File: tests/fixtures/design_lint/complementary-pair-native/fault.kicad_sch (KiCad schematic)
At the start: 1 part, among them J1 Synthetic USB SuperSpeed conn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

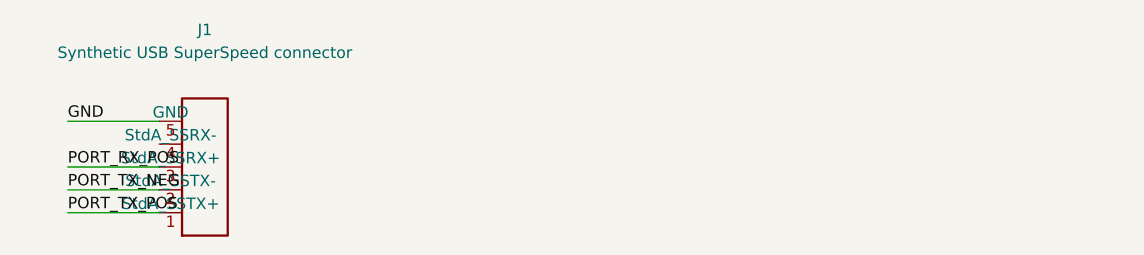
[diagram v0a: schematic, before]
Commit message: feat: recognize Ethernet complementary pair aliases
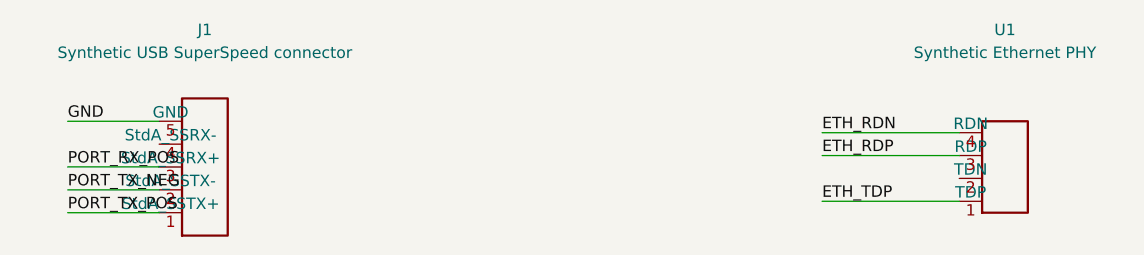
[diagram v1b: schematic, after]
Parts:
- added U1: Synthetic Ethernet PHY, Synthetic:EthernetPhy, symbol Synthetic:EthernetPhy
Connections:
- new net ETH_RDN: U1.4 (RDN)
- new net ETH_RDP: U1.3 (RDP)
- new net ETH_TDP: U1.1 (TDP)
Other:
- title: USB SuperSpeed pair fault -> USB and Ethernet pair fault
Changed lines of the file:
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@@
 (kicad_sch (version 20231120) (generator "eeschema")
   (paper "A4")
-  (title_block (title "USB SuperSpeed pair fault")
+  (title_block (title "USB and Ethernet pair fault")
     (comment 1 "NOT FOR MANUFACTURE - synthetic tooling fixture"))
   (symbol (lib_id "Synthetic:UsbSuperSpeedPort") (at 76.20 76.20 0) (unit 1)
@@
     (pin "4")
     (pin "5")
-    (instances (project "Synthetic USB SuperSpeed pair fault" (path "/76332122-47cd-5a8b-95f1-09d5560f0487" (reference "J1") (unit 1)))))
+    (instances (project "USB and Ethernet pair fault" (path "/76332122-47cd-5a8b-95f1-09d5560f0487" (reference "J1") (unit 1)))))
+  (symbol (lib_id "Synthetic:EthernetPhy") (at 165.10 76.20 0) (unit 1)
+    (in_bom yes) (on_board yes) (dnp no)
+    (property "Reference" "U1" (at 165.10 60.96 0) (effects (font (size 1.27 1.27))))
+    (property "Value" "Synthetic Ethernet PHY" (at 165.10 63.50 0) (effects (font (size 1.27 1.27))))
+    (property "Footprint" "Synthetic:EthernetPhy" (at 165.10 76.20 0) (effects (font (size 1.27 1.27)) hide))
+    (property "Datasheet" "" (at 165.10 76.20 0) (effects (font (size 1.27 1.27)) hide))
+    (pin "1")
+    (pin "2")
+    (pin "3")
+    (pin "4")
+    (instances (project "USB and Ethernet pair fault" (path "/76332122-47cd-5a8b-95f1-09d5560f0487" (reference "U1") (unit 1)))))
   (wire (pts (xy 71.12 81.28) (xy 60.96 81.28))
     (stroke (width 0) (type default))
@@
     (effects (font (size 1.27 1.27)) (justify left bottom))
 )
+  (wire (pts (xy 160.02 80.01) (xy 144.78 80.01))
+    (stroke (width 0) (type default)))
+  (wire (pts (xy 160.02 74.93) (xy 144.78 74.93))
+    (stroke (width 0) (type default)))
+  (wire (pts (xy 160.02 72.39) (xy 144.78 72.39))
+    (stroke (width 0) (type default)))
+  (label "ETH_TDP" (at 144.78 80.01 0)
+    (effects (font (size 1.27 1.27)) (justify left bottom))
+)
+  (label "ETH_RDP" (at 144.78 74.93 0)
+    (effects (font (size 1.27 1.27)) (justify left bottom))
+)
+  (label "ETH_RDN" (at 144.78 72.39 0)
+    (effects (font (size 1.27 1.27)) (justify left bottom))
+)

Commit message: test: isolate complementary pair native control
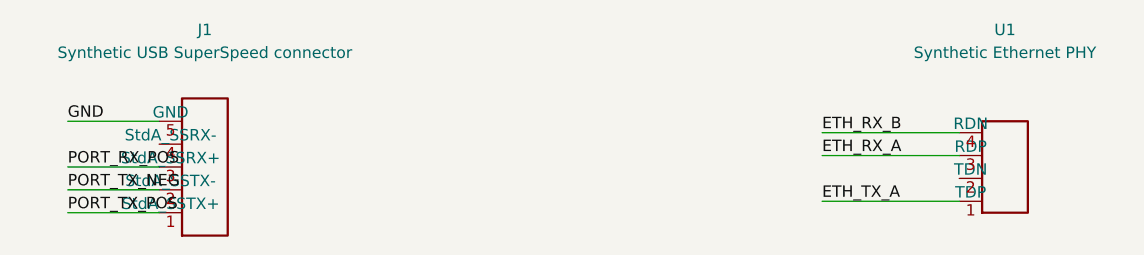
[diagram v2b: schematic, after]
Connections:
- net ETH_RDN renamed ETH_RX_B
- net ETH_RDP renamed ETH_RX_A
- net ETH_TDP renamed ETH_TX_A
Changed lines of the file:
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@@
   (wire (pts (xy 160.02 72.39) (xy 144.78 72.39))
     (stroke (width 0) (type default)))
-  (label "ETH_TDP" (at 144.78 80.01 0)
+  (label "ETH_TX_A" (at 144.78 80.01 0)
     (effects (font (size 1.27 1.27)) (justify left bottom))
 )
-  (label "ETH_RDP" (at 144.78 74.93 0)
+  (label "ETH_RX_A" (at 144.78 74.93 0)
     (effects (font (size 1.27 1.27)) (justify left bottom))
 )
-  (label "ETH_RDN" (at 144.78 72.39 0)
+  (label "ETH_RX_B" (at 144.78 72.39 0)
     (effects (font (size 1.27 1.27)) (justify left bottom))
 )
